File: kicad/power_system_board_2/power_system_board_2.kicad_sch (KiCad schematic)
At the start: 21 parts, among them J1 USB_C_Receptacle_USB2.0_16P, J2 Conn_01x04_Pin, Q1 NMOS, Q3 PMOS, U1 ${SIM.PARAMS}

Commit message: Pushing a few more changes so I have everything
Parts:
- U1: value ${SIM.PARAMS} -> LM358
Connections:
- net Vtest: now reaches R3.2, R4.1, U1.2 (-)
- net Vref: now reaches D1.1 (K), R6.2, U1.1 (+)
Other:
- note added: "UVLO operation - Gate is more negative than source => PMOS is on - Vopamp = A(Vref - Vtest) - If Vtest > Vref, the opamp should stay 0, and the PMOS = on"
- note removed: "UVLO If (Voutvalue - Vtestvalue) <= 0 then the pmos turns off"
- moved on the sheet: D1, Q3, R3, R4, R5, R6, R7, R8, U1

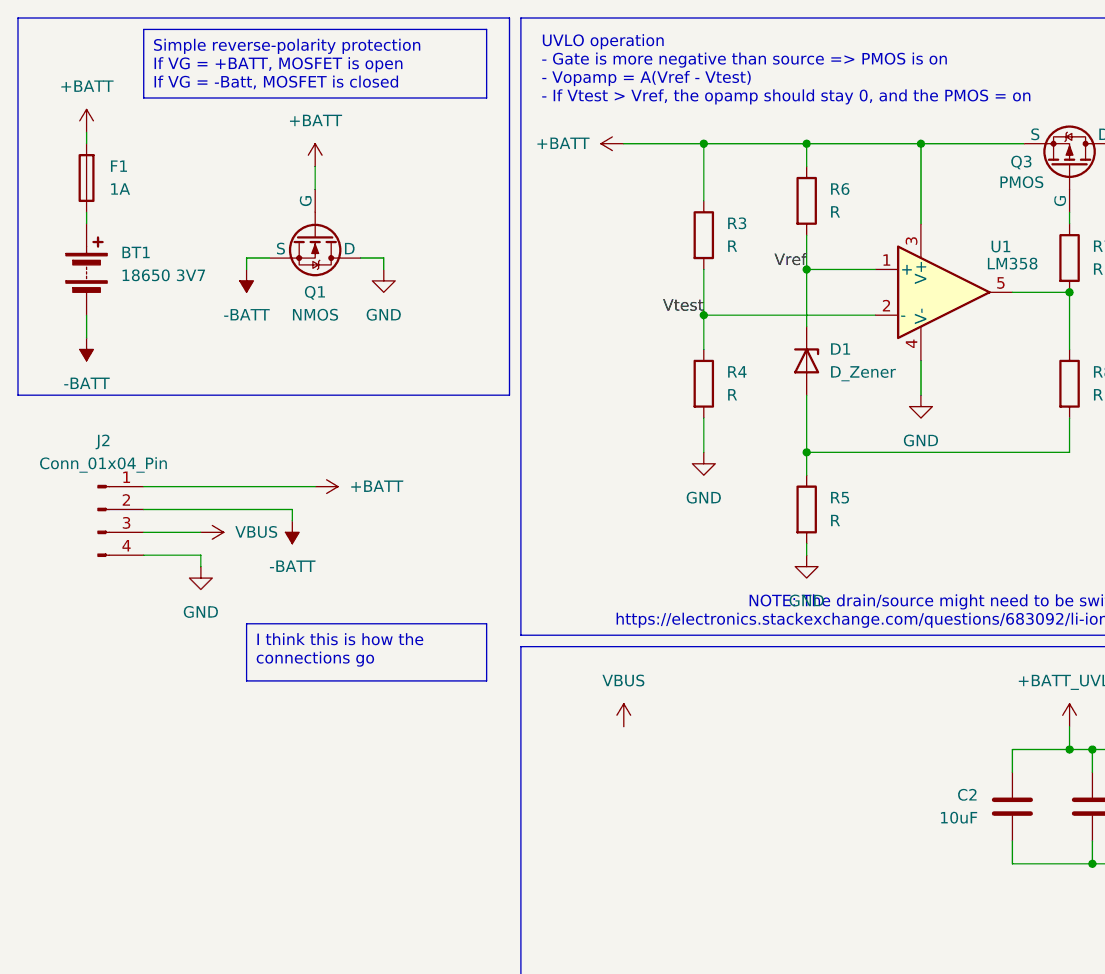
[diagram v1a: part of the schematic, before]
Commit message: Testing some file system stuff. Addition to the power design
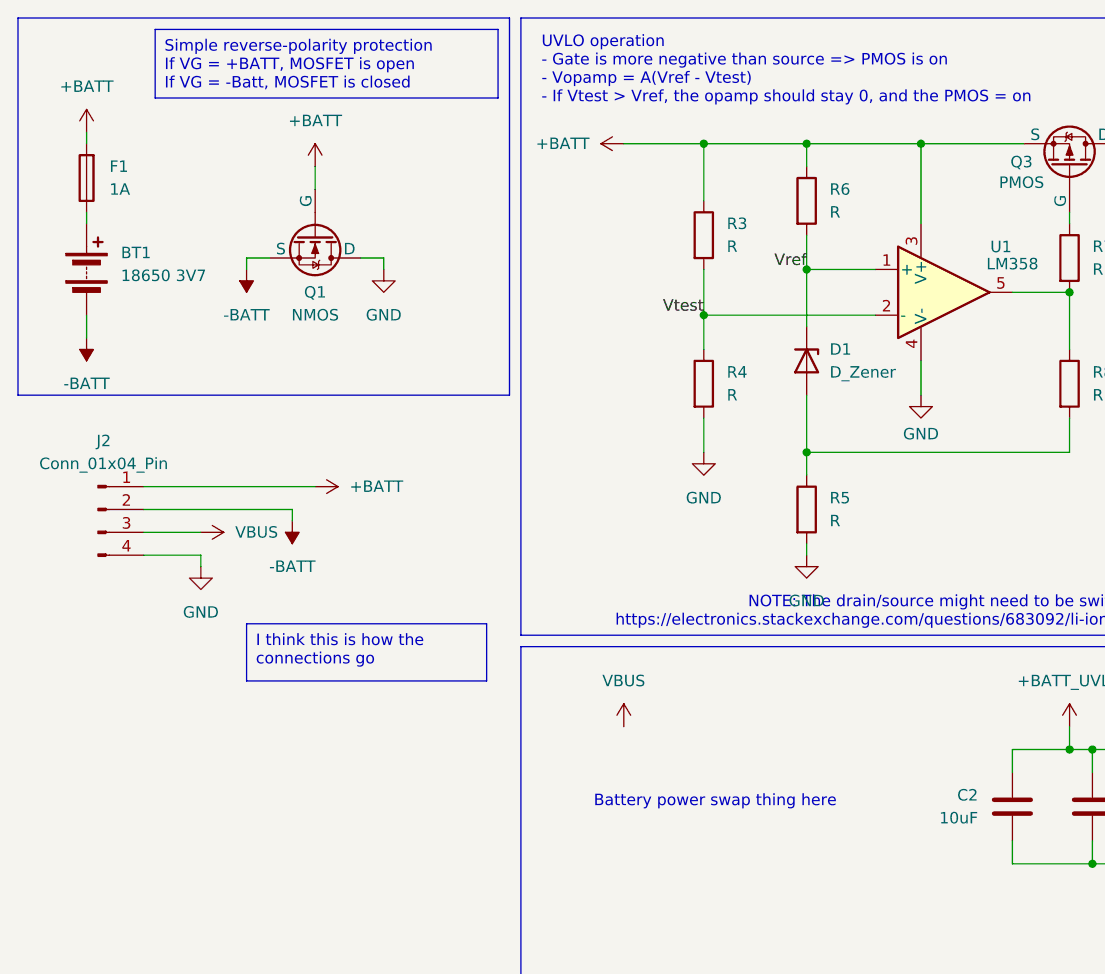
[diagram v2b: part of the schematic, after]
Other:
- note added: "Battery power swap thing here"
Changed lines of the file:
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@@
 	(text_box "Simple reverse-polarity protection\nIf VG = +BATT, MOSFET is open\nIf VG = -Batt, MOSFET is closed\n"
 		(exclude_from_sim no)
-		(at 26.67 13.97 0)
+		(at 27.94 13.97 0)
 		(size 38.1 7.62)
 		(stroke
@@
 		)
 	)
+	(text "Battery power swap thing here"
+		(exclude_from_sim no)
+		(at 90.17 99.822 0)
+		(effects
+			(font
+				(size 1.27 1.27)
+			)
+		)
+	)
 	(text "Read sheet when assembling"
 		(exclude_from_sim no)
@@
 		(on_board yes)
 		(dnp no)
-		(fields_autoplaced yes)
 		(property "Reference" "#PWR05"
 			(at 113.03 60.96 0)
@@
 		)
 		(property "Value" "GND"
-			(at 113.03 59.69 0)
+			(at 113.03 58.928 0)
 			(effects
 				(font
@@
 			)
 		)
-		(property "Datasheet" "https://ngspice.sourceforge.io/docs/ngspice-html-manual/manual.xhtml#sec__SUBCKT_Subcircuits"
+		(property "Datasheet" "https://www.ti.com/lit/ds/symlink/lm358.pdf?ts=1712884954575&ref_url=https%253A%252F%252Fwww.ti.com%252Fproduct%252Fzh-tw%252FLM358"
 			(at 115.57 43.18 0)
 			(effects

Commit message: BOM updates harry
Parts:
- Q1: value NMOS -> NMOS - VN0109N3
- Q3: value PMOS -> PMOS - VP0106N3
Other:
- note added: "Using BZX83C2V4 for the zener (Communica)"
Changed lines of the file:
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@@
+		)
+	)
+	(text "Using BZX83C2V4 for the zener\n(Communica)"
+		(exclude_from_sim no)
+		(at 125.73 68.072 0)
+		(effects
+			(font
+				(size 1.27 1.27)
+			)
 		)
 	)
@@
 		(on_board yes)
 		(dnp no)
-		(fields_autoplaced yes)
 		(property "Reference" "Q1"
 			(at 45.72 43.18 90)
@@
 			)
 		)
-		(property "Value" "NMOS"
-			(at 45.72 45.72 90)
+		(property "Value" "NMOS - VN0109N3"
+			(at 45.72 48.006 90)
 			(effects
 				(font
@@
 			)
 		)
-		(property "Value" "PMOS"
-			(at 124.206 30.988 90)
-			(effects
-				(font
+		(property "Value" "PMOS - VP0106N3"
+			(at 140.97 31.75 90)
+			(effects
+				(font
